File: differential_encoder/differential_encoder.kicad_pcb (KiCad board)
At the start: 2 copper layers, 99.8 x 40.4 mm, 73 parts, among them J101 Conn_01x12, J102 RJ45_LED_Shielded, J103 RJ45_LED_Shielded, Q101 Q_NMOS_GSD, Q102 Q_NMOS_GSD, Q103 Q_NMOS_GSD, Q104 Q_NMOS_GSD, Q105 Q_NMOS_GSD, Q106 Q_NMOS_GSD, U101 MAX489E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

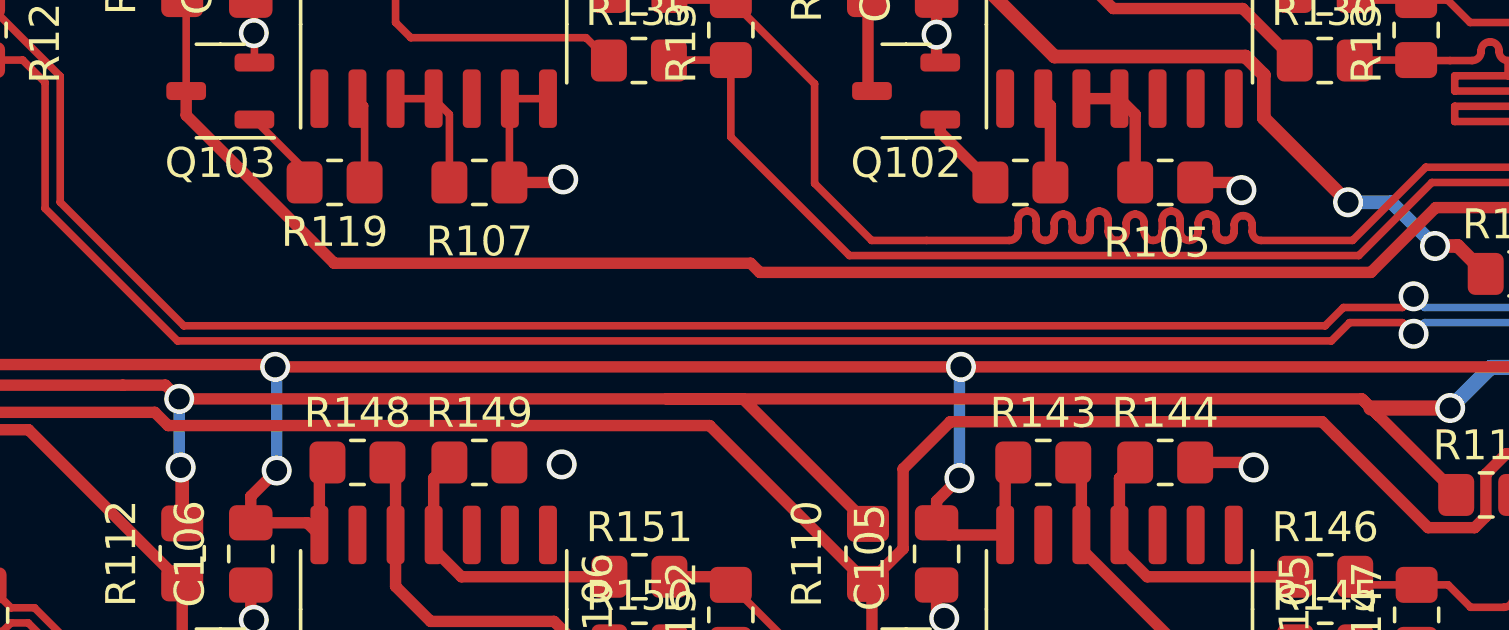
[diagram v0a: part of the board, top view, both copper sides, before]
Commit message: finished the encoder tracing
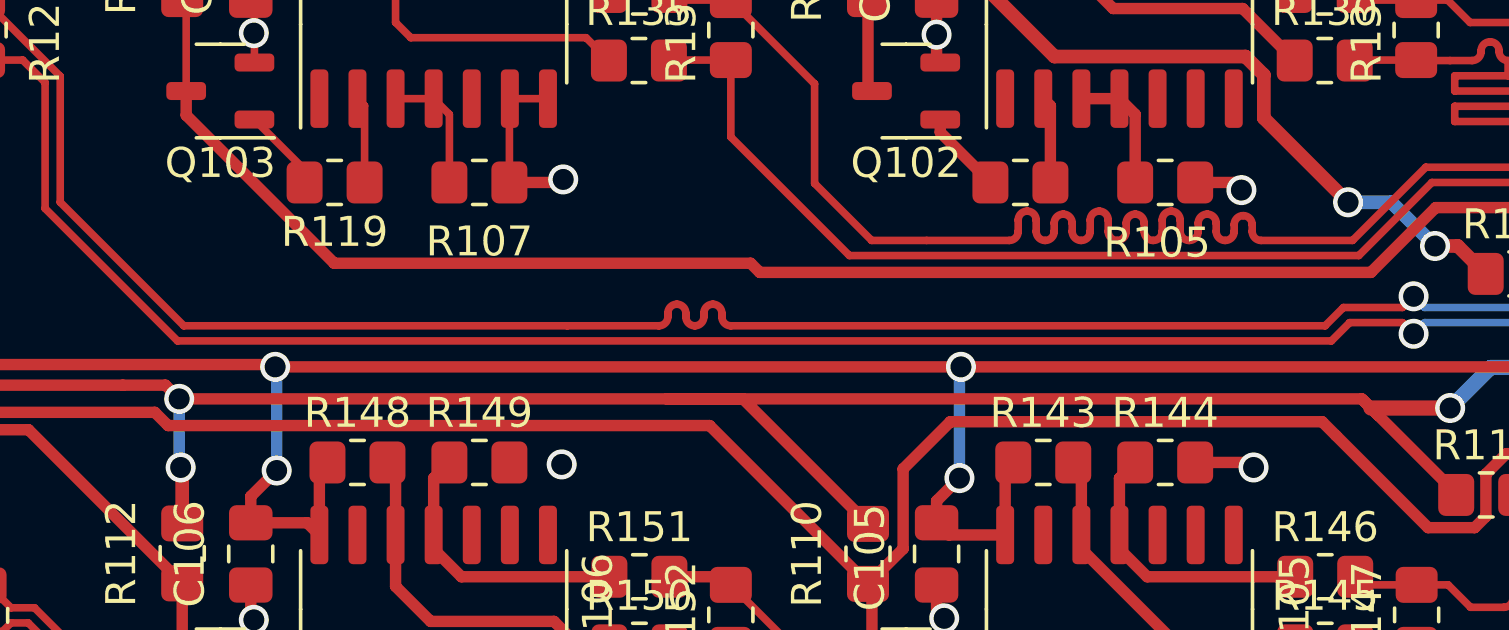
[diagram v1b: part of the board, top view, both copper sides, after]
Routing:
- net a1-: track 72.7 -> 74.4 mm
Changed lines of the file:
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@@
   (segment (start 160.929365 86.869981) (end 159.310635 86.869981) (width 0.254) (layer "B.Cu") (net 16))
   (segment (start 165.386109 82.685) (end 165.270582 82.685) (width 0.254) (layer "B.Cu") (net 16))
-  (segment (start 149.958818 85.9556) (end 149.349218 86.5652) (width 0.254) (layer "F.Cu") (net 17))
-  (segment (start 151.9254 85.9556) (end 149.958818 85.9556) (width 0.254) (layer "F.Cu") (net 17))
+  (segment (start 128.04 86.2652) (end 128.04 86.14605) (width 0.254) (layer "F.Cu") (net 17))
+  (segment (start 149.349218 86.5652) (end 129.54 86.5652) (width 0.254) (layer "F.Cu") (net 17))
+  (segment (start 128.64 86.146056) (end 128.64 86.2652) (width 0.254) (layer "F.Cu") (net 17))
   (segment (start 107.186 78.246) (end 104.648 75.708) (width 0.254) (layer "F.Cu") (net 17))
-  (segment (start 107.186 82.445618) (end 107.186 78.246) (width 0.254) (layer "F.Cu") (net 17))
   (segment (start 111.305582 86.5652) (end 107.186 82.445618) (width 0.254) (layer "F.Cu") (net 17))
+  (segment (start 124.09 86.5652) (end 111.305582 86.5652) (width 0.254) (layer "F.Cu") (net 17))
   (segment locked (start 102.87 75.708) (end 102.6 75.438) (width 0.254) (layer "F.Cu") (net 17))
   (segment locked (start 104.648 75.708) (end 102.87 75.708) (width 0.254) (layer "F.Cu") (net 17))
+  (segment (start 129.24 86.2652) (end 129.24 86.146056) (width 0.254) (layer "F.Cu") (net 17))
+  (segment (start 127.44 86.14605) (end 127.44 86.2652) (width 0.254) (layer "F.Cu") (net 17))
+  (segment (start 151.9254 85.9556) (end 149.958818 85.9556) (width 0.254) (layer "F.Cu") (net 17))
+  (segment (start 127.14 86.5652) (end 124.09 86.5652) (width 0.254) (layer "F.Cu") (net 17))
+  (segment (start 149.958818 85.9556) (end 149.349218 86.5652) (width 0.254) (layer "F.Cu") (net 17))
+  (segment (start 107.186 82.445618) (end 107.186 78.246) (width 0.254) (layer "F.Cu") (net 17))
   (segment (start 152.2984 85.5826) (end 151.9254 85.9556) (width 0.254) (layer "F.Cu") (net 17))
-  (segment (start 149.349218 86.5652) (end 111.305582 86.5652) (width 0.254) (layer "F.Cu") (net 17))
   (via (at 152.2984 85.5826) (size 1) (drill 0.7) (layers "F.Cu" "B.Cu") (net 17))
+  (arc (start 128.34 86.5652) (mid 128.127868 86.477332) (end 128.04 86.2652) (width 0.254) (layer "F.Cu") (net 17))
+  (arc (start 128.64 86.2652) (mid 128.552132 86.477332) (end 128.34 86.5652) (width 0.254) (layer "F.Cu") (net 17))
+  (arc (start 127.44 86.2652) (mid 127.352132 86.477332) (end 127.14 86.5652) (width 0.254) (layer "F.Cu") (net 17))
+  (arc (start 128.94 85.846056) (mid 128.727868 85.933924) (end 128.64 86.146056) (width 0.254) (layer "F.Cu") (net 17))
+  (arc (start 127.74 85.84605) (mid 127.527868 85.933918) (end 127.44 86.14605) (width 0.254) (layer "F.Cu") (net 17))
+  (arc (start 128.04 86.14605) (mid 127.952132 85.933918) (end 127.74 85.84605) (width 0.254) (layer "F.Cu") (net 17))
+  (arc (start 129.24 86.146056) (mid 129.152132 85.933924) (end 128.94 85.846056) (width 0.254) (layer "F.Cu") (net 17))
+  (arc (start 129.54 86.5652) (mid 129.327868 86.477332) (end 129.24 86.2652) (width 0.254) (layer "F.Cu") (net 17))
   (segment (start 165.07 81.738) (end 165.07 82.172818) (width 0.254) (layer "B.Cu") (net 17))
   (segment (start 161.13101 85.9556) (end 160.72061 86.366) (width 0.254) (layer "B.Cu") (net 17))
